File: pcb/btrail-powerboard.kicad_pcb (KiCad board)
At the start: 2 copper layers, 44.5 x 52.8 mm, 13 parts, among them J1 RJ45_Shielded, Q1 IRLZ34N, Q2 IRLZ34N

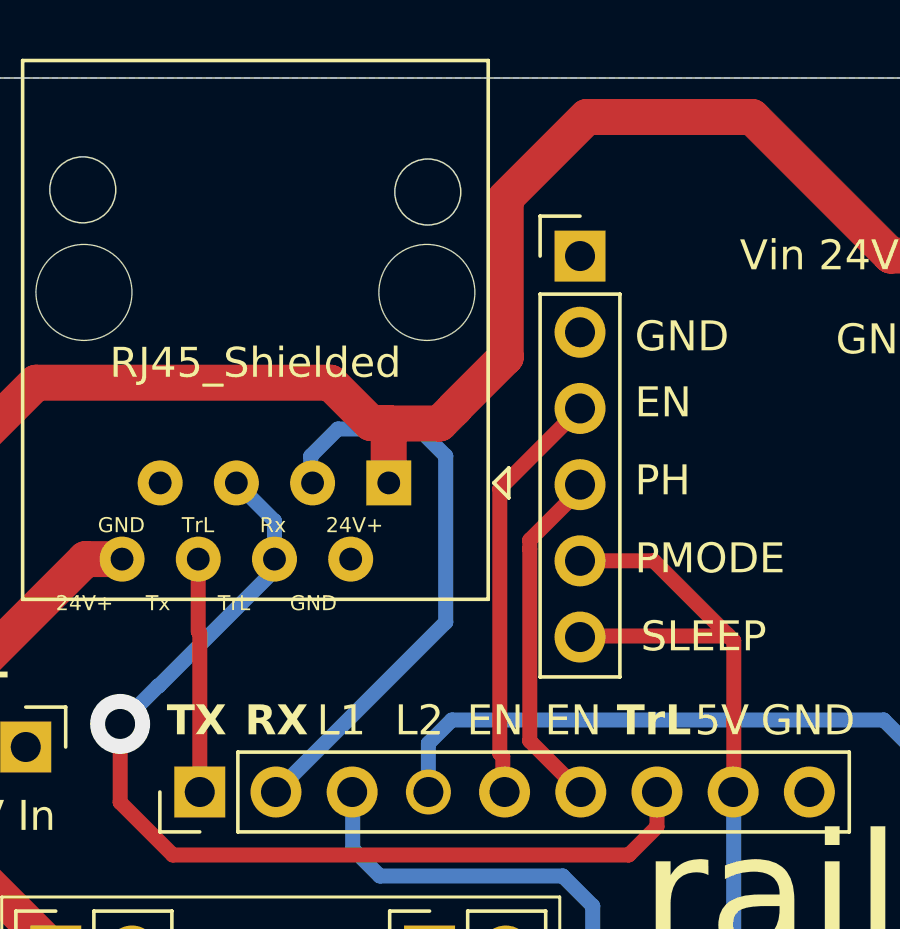
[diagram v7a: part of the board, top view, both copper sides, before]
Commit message: Quick 24V trace fix
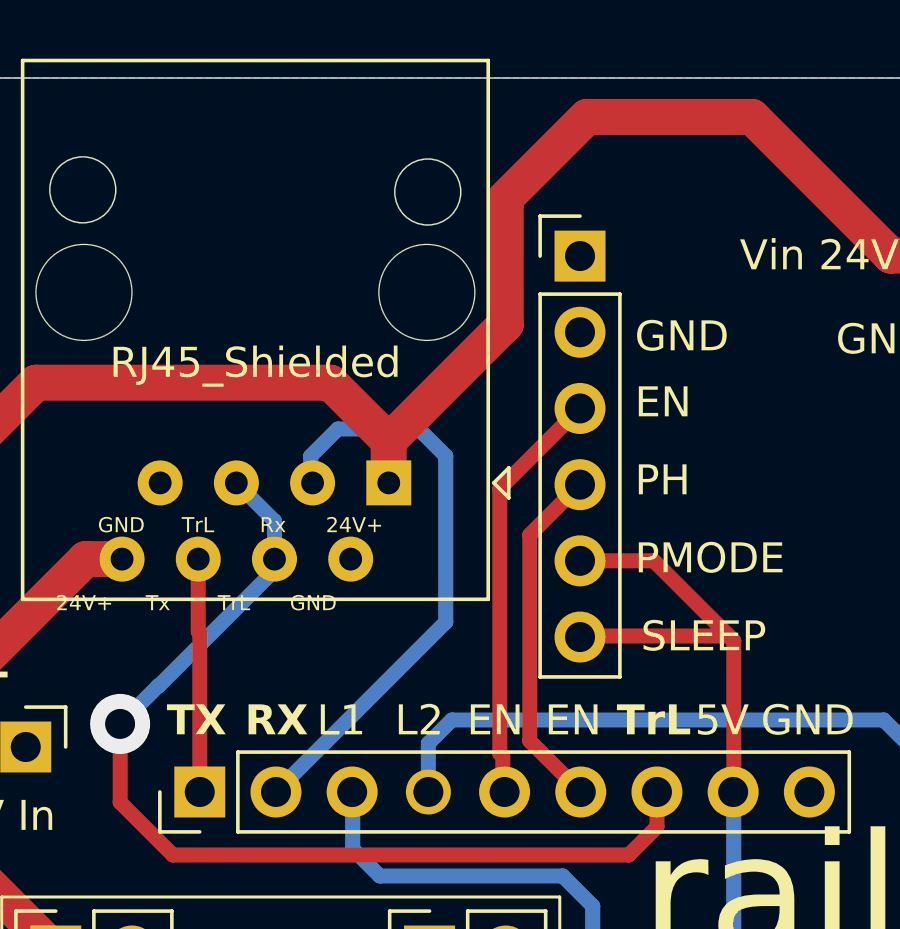
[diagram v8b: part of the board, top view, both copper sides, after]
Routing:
- net +24V: track 133.3 -> 132.6 mm
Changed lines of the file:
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@@
+	)
+	(segment
+		(start 233.226 27.584)
+		(end 233.1 27.584)
+		(width 1.2)
+		(layer "F.Cu")
+		(net 2)
+	)
+	(segment
+		(start 233.1 63.5)
+		(end 233.1 33.150553)
+		(width 1.2)
+		(layer "F.Cu")
+		(net 2)
+	)
+	(segment
+		(start 233.1 33.150553)
+		(end 233.226 33.024553)
+		(width 1.2)
+		(layer "F.Cu")
+		(net 2)
+	)
+	(segment
+		(start 225.555 66)
+		(end 230.6 66)
+		(width 1.2)
+		(layer "F.Cu")
+		(net 2)
+	)
+	(segment
+		(start 233.226 33.024553)
+		(end 233.226 27.584)
+		(width 1.2)
+		(layer "F.Cu")
+		(net 2)
+	)
+	(segment
+		(start 231.4 61.1)
+		(end 233.1 59.4)
+		(width 1.2)
+		(layer "F.Cu")
+		(net 2)
+	)
+	(segment
+		(start 219.612073 19.7)
+		(end 214.1 19.7)
+		(width 1.2)
+		(layer "F.Cu")
+		(net 2)
+	)
+	(segment
+		(start 232.08 24.32)
+		(end 224.232073 24.32)
+		(width 1.2)
+		(layer "F.Cu")
+		(net 2)
 	)
 	(segment
@@
 	)
 	(segment
+		(start 192.86 40.7)
+		(end 192.86 38.9675)
+		(width 1.2)
+		(layer "F.Cu")
+		(net 2)
+	)
+	(segment
+		(start 230.5 61.1)
+		(end 231.4 61.1)
+		(width 1.2)
+		(layer "F.Cu")
+		(net 2)
+	)
+	(segment
+		(start 233.1 27.584)
+		(end 233.1 25.34)
+		(width 1.2)
+		(layer "F.Cu")
+		(net 2)
+	)
+	(segment
+		(start 198.94 47.5)
+		(end 196.4 47.5)
+		(width 1.2)
+		(layer "F.Cu")
+		(net 2)
+	)
+	(segment
+		(start 192.86 31.44)
+		(end 192.86 43.96)
+		(width 1.2)
+		(layer "F.Cu")
+		(net 2)
+	)
+	(segment
+		(start 205.55676 28.55676)
+		(end 195.74324 28.55676)
+		(width 1.2)
+		(layer "F.Cu")
+		(net 2)
+	)
+	(segment
 		(start 230.6 66)
 		(end 233.1 63.5)
@@
 	)
 	(segment
-		(start 205.55676 28.55676)
-		(end 195.74324 28.55676)
-		(width 1.2)
-		(layer "F.Cu")
-		(net 2)
-	)
-	(segment
-		(start 207.5 29.9)
-		(end 206.9 29.9)
-		(width 1.2)
-		(layer "F.Cu")
-		(net 2)
-	)
-	(segment
-		(start 231.4 61.1)
-		(end 233.1 59.4)
-		(width 1.2)
-		(layer "F.Cu")
-		(net 2)
-	)
-	(segment
-		(start 209.7 29.410642)
-		(end 209.193265 29.917377)
-		(width 1.2)
-		(layer "F.Cu")
-		(net 2)
-	)
-	(segment
-		(start 211.4 27.7)
-		(end 209.7 29.4)
+		(start 192.86 43.96)
+		(end 196.4 47.5)
+		(width 1.2)
+		(layer "F.Cu")
+		(net 2)
+	)
+	(segment
+		(start 207.5 30.5)
+		(end 205.55676 28.55676)
+		(width 1.2)
+		(layer "F.Cu")
+		(net 2)
+	)
+	(segment
+		(start 207.5 31.8975)
+		(end 207.5 30.5)
+		(width 1.2)
+		(layer "F.Cu")
+		(net 2)
+	)
+	(segment
+		(start 192.86 38.9675)
+		(end 197.39 34.4375)
 		(width 1.2)
 		(layer "F.Cu")
@@
 	(segment
 		(start 211.4 22.4)
-		(end 211.4 27.7)
-		(width 1.2)
-		(layer "F.Cu")
-		(net 2)
-	)
-	(segment
-		(start 206.9 29.9)
-		(end 205.55676 28.55676)
+		(end 211.4 26.6)
+		(width 1.2)
+		(layer "F.Cu")
+		(net 2)
+	)
+	(segment
+		(start 207.5 30.5)
+		(end 211.4 26.6)
+		(width 1.2)
+		(layer "F.Cu")
+		(net 2)
+	)
+	(segment
+		(start 224.232073 24.32)
+		(end 219.612073 19.7)
 		(width 1.2)
 		(layer "F.Cu")
@@
 	)
 	(segment
-		(start 192.86 43.96)
-		(end 196.4 47.5)
-		(width 1.2)
-		(layer "F.Cu")
-		(net 2)
-	)
-	(segment
-		(start 192.86 40.7)
-		(end 192.86 38.9675)
-		(width 1.2)
-		(layer "F.Cu")
-		(net 2)
-	)
-	(segment
-		(start 209.7 29.4)
-		(end 209.7 29.410642)
-		(width 1.2)
-		(layer "F.Cu")
-		(net 2)
-	)
-	(segment
-		(start 233.1 63.5)
-		(end 233.1 33.150553)
-		(width 1.2)
-		(layer "F.Cu")
-		(net 2)
-	)
-	(segment
-		(start 230.5 61.1)
-		(end 231.4 61.1)
-		(width 1.2)
-		(layer "F.Cu")
-		(net 2)
-	)
-	(segment
 		(start 195.74324 28.55676)
 		(end 192.86 31.44)
@@
 	)
 	(segment
-		(start 198.94 47.5)
-		(end 196.4 47.5)
-		(width 1.2)
-		(layer "F.Cu")
-		(net 2)
-	)
-	(segment
-		(start 233.226 33.024553)
-		(end 233.226 27.584)
-		(width 1.2)
-		(layer "F.Cu")
-		(net 2)
-	)
-	(segment
-		(start 232.08 24.32)
-		(end 224.232073 24.32)
-		(width 1.2)
-		(layer "F.Cu")
-		(net 2)
-	)
-	(segment
-		(start 192.86 38.9675)
-		(end 197.39 34.4375)
-		(width 1.2)
-		(layer "F.Cu")
-		(net 2)
-	)
-	(segment
-		(start 192.86 31.44)
-		(end 192.86 43.96)
-		(width 1.2)
-		(layer "F.Cu")
-		(net 2)
-	)
-	(segment
-		(start 224.232073 24.32)
-		(end 219.612073 19.7)
-		(width 1.2)
-		(layer "F.Cu")
-		(net 2)
-	)
-	(segment
-		(start 233.1 27.584)
-		(end 233.1 25.34)
-		(width 1.2)
-		(layer "F.Cu")
-		(net 2)
-	)
-	(segment
-		(start 225.555 66)
-		(end 230.6 66)
-		(width 1.2)
-		(layer "F.Cu")
-		(net 2)
-	)
-	(segment
-		(start 207.5 31.8975)
-		(end 207.5 29.9)
-		(width 1.2)
-		(layer "F.Cu")
-		(net 2)
-	)
-	(segment
-		(start 209.193265 29.917377)
-		(end 207.517377 29.917377)
-		(width 1.2)
-		(layer "F.Cu")
-		(net 2)
-	)
-	(segment
-		(start 219.612073 19.7)
-		(end 214.1 19.7)
-		(width 1.2)
-		(layer "F.Cu")
-		(net 2)
-	)
-	(segment
-		(start 233.226 27.584)
-		(end 233.1 27.584)
-		(width 1.2)
-		(layer "F.Cu")
-		(net 2)
-	)
-	(segment
-		(start 207.517377 29.917377)
-		(end 207.5 29.9)
-		(width 1.2)
-		(layer "F.Cu")
-		(net 2)
-	)
-	(segment
 		(start 197.39 34.4375)
 		(end 198.61 34.4375)
@@
 	)
 	(segment
-		(start 233.1 33.150553)
-		(end 233.226 33.024553)
-		(width 1.2)
-		(layer "F.Cu")
-		(net 2)
-	)
-	(segment
 		(start 211.3 42.06)
 		(end 211.3 41.015628)
@@
 	)
 	(segment
-		(start 212.2 33.8)
-		(end 213.43 32.57)
+		(start 212.2 33.63)
+		(end 213.875 31.955)
 		(width 0.5)
 		(layer "F.Cu")
@@
 	)
 	(segment
-		(start 213.43 32.57)
-		(end 213.43 32.4)
-		(width 0.5)
-		(layer "F.Cu")
-		(net 7)
-	)
-	(segment
 		(start 212.2 40.5)
-		(end 212.2 34.1)
-		(width 0.5)
-		(layer "F.Cu")
-		(net 7)
-	)
-	(segment
-		(start 213.43 32.4)
-		(end 213.875 31.955)
-		(width 0.5)
-		(layer "F.Cu")
-		(net 7)
-	)
-	(segment
-		(start 212.2 34.1)
-		(end 212.2 33.8)
-		(width 0.5)
-		(layer "F.Cu")
+		(end 212.2 33.63)
+		(width 0.5)
+		(layer "F.Cu")
